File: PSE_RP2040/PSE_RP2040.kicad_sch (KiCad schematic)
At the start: 69 parts, among them J1 USB_B, J2 USB_B_Mini, J3 8P8C_LED, J4 Conn_01x03, Q2 IRLML6402, SW1 SW_Push, SW2 SW_Push, U1 RP2040, U2 PCF8563T, U5 W25Q16JVUSSQ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

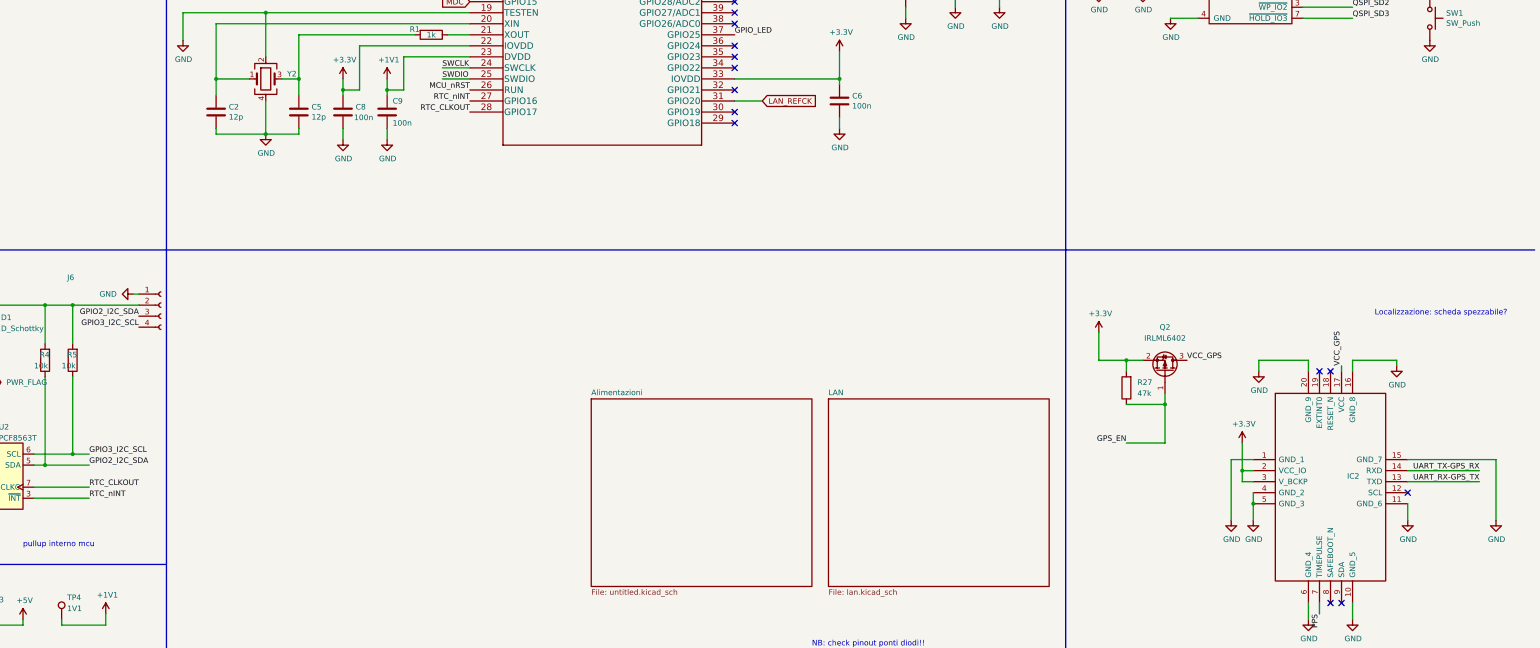
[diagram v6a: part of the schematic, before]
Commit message: piazzamento componenti pcb
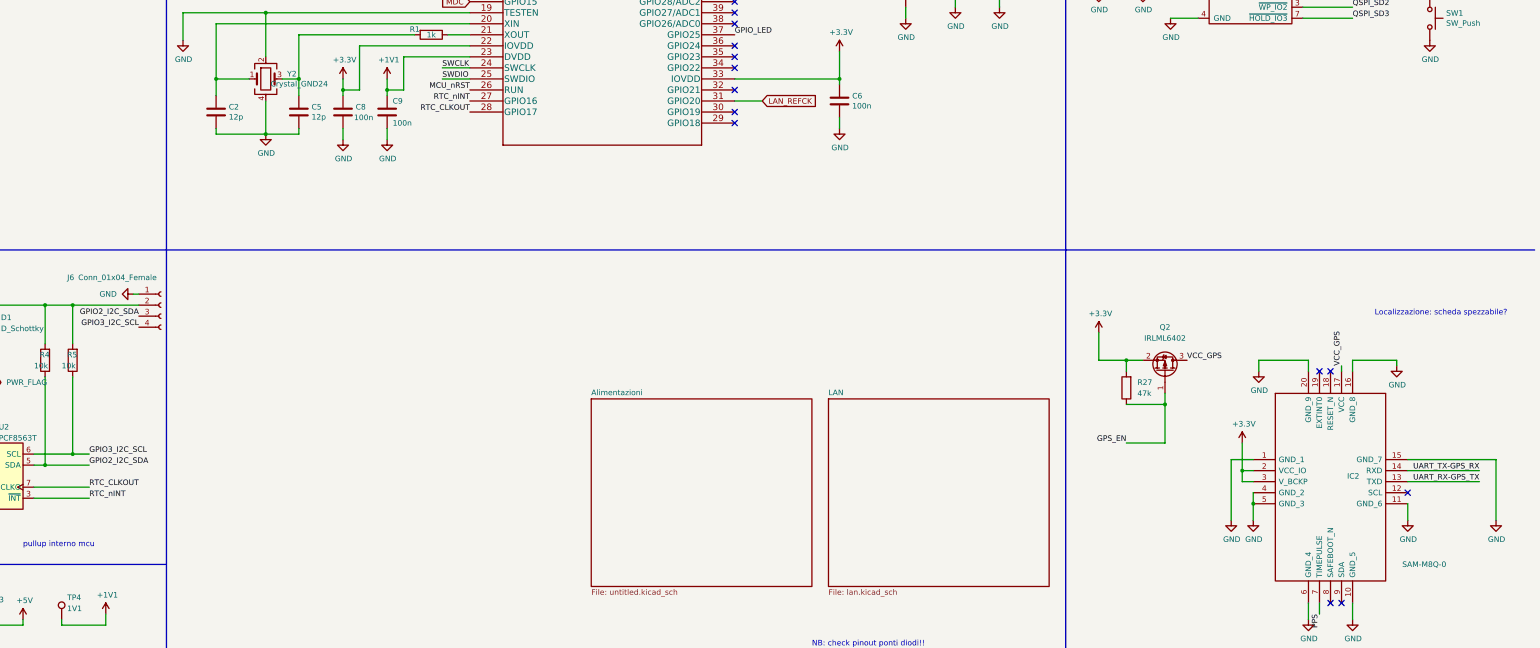
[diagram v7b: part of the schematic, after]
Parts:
- IC2: value (none) -> SAM-M8Q-0; footprint (none) -> PSE2021:SAM-M8Q
- J6: value (none) -> Conn_01x04_Female; footprint (none) -> Connector_PinHeader_2.54mm:PinHeader_1x04_P2.54mm_Vertical
- SW1, SW2: footprint (none) -> Button_Switch_THT:SW_PUSH_6mm
- TP1, TP2: footprint (none) -> TestPoint:TestPoint_Loop_D1.80mm_Drill1.0mm_Beaded
- TP10, TP11, TP12, TP13, TP3, TP4, TP5, TP6, TP7, TP8, TP9: footprint (none) -> TestPoint:TestPoint_Pad_D1.0mm
- Y2: value (none) -> Crystal_GND24; footprint (none) -> Crystal:Crystal_SMD_3225-4Pin_3.2x2.5mm
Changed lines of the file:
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@@
       (effects (font (size 1.27 1.27)) (justify left))
     )
-    (property "Value" "" (id 1) (at 116.6876 87.503 0)
-      (effects (font (size 1.27 1.27)) (justify left))
-    )
-    (property "Footprint" "" (id 2) (at 115.57 86.36 0)
+    (property "Value" "Crystal_GND24" (id 1) (at 116.6876 87.503 0)
+      (effects (font (size 1.27 1.27)) (justify left))
+    )
+    (property "Footprint" "Crystal:Crystal_SMD_3225-4Pin_3.2x2.5mm" (id 2) (at 115.57 86.36 0)
       (effects (font (size 1.27 1.27)) hide)
     )
@@
       (effects (font (size 1.27 1.27)) (justify left))
     )
-    (property "Footprint" "" (id 2) (at 388.62 72.39 0)
+    (property "Footprint" "Button_Switch_THT:SW_PUSH_6mm" (id 2) (at 388.62 72.39 0)
       (effects (font (size 1.27 1.27)) hide)
     )
@@
       (effects (font (size 1.27 1.27)) (justify left))
     )
-    (property "Footprint" "" (id 2) (at 43.18 210.82 0)
+    (property "Footprint" "TestPoint:TestPoint_Loop_D1.80mm_Drill1.0mm_Beaded" (id 2) (at 43.18 210.82 0)
       (effects (font (size 1.27 1.27)) hide)
     )
@@
       (effects (font (size 1.27 1.27)) (justify left))
     )
-    (property "Footprint" "" (id 2) (at 73.66 238.76 0)
+    (property "Footprint" "TestPoint:TestPoint_Pad_D1.0mm" (id 2) (at 73.66 238.76 0)
       (effects (font (size 1.27 1.27)) hide)
     )
@@
       (effects (font (size 1.27 1.27)) (justify left))
     )
-    (property "Footprint" "" (id 2) (at 24.13 255.27 0)
+    (property "Footprint" "TestPoint:TestPoint_Pad_D1.0mm" (id 2) (at 24.13 255.27 0)
       (effects (font (size 1.27 1.27)) hide)
     )
@@
       (effects (font (size 1.27 1.27)) (justify left))
     )
-    (property "Footprint" "" (id 2) (at 24.13 210.82 0)
+    (property "Footprint" "TestPoint:TestPoint_Loop_D1.80mm_Drill1.0mm_Beaded" (id 2) (at 24.13 210.82 0)
       (effects (font (size 1.27 1.27)) hide)
     )
@@
       (effects (font (size 1.27 1.27)) (justify left))
     )
-    (property "Footprint" "" (id 2) (at 24.13 238.76 0)
+    (property "Footprint" "TestPoint:TestPoint_Pad_D1.0mm" (id 2) (at 24.13 238.76 0)
       (effects (font (size 1.27 1.27)) hide)
     )
@@
       (effects (font (size 1.27 1.27)) (justify left))
     )
-    (property "Footprint" "" (id 2) (at 80.01 224.79 0)
+    (property "Footprint" "TestPoint:TestPoint_Pad_D1.0mm" (id 2) (at 80.01 224.79 0)
       (effects (font (size 1.27 1.27)) hide)
     )
@@
       (effects (font (size 1.27 1.27)) (justify left))
     )
-    (property "Footprint" "" (id 2) (at 63.5 224.79 0)
+    (property "Footprint" "TestPoint:TestPoint_Pad_D1.0mm" (id 2) (at 63.5 224.79 0)
       (effects (font (size 1.27 1.27)) hide)
     )
@@
       (effects (font (size 1.27 1.27)) (justify left))
     )
-    (property "Footprint" "" (id 2) (at 44.45 226.06 0)
+    (property "Footprint" "TestPoint:TestPoint_Pad_D1.0mm" (id 2) (at 44.45 226.06 0)
       (effects (font (size 1.27 1.27)) hide)
     )
@@
       (effects (font (size 1.27 1.27)) (justify left))
     )
-    (property "Footprint" "" (id 2) (at 73.66 210.82 0)
+    (property "Footprint" "TestPoint:TestPoint_Pad_D1.0mm" (id 2) (at 73.66 210.82 0)
       (effects (font (size 1.27 1.27)) hide)
     )
@@
       (effects (font (size 1.27 1.27)) (justify left))
     )
-    (property "Footprint" "" (id 2) (at 111.76 39.37 0)
+    (property "Footprint" "Button_Switch_THT:SW_PUSH_6mm" (id 2) (at 111.76 39.37 0)
       (effects (font (size 1.27 1.27)) hide)
     )
@@
       (effects (font (size 1.27 1.27)) (justify left))
     )
-    (property "Footprint" "" (id 2) (at 24.13 226.06 0)
+    (property "Footprint" "TestPoint:TestPoint_Pad_D1.0mm" (id 2) (at 24.13 226.06 0)
       (effects (font (size 1.27 1.27)) hide)
     )
@@
       (effects (font (size 1.27 1.27)) (justify left))
     )
-    (property "Value" "" (id 1) (at 377.19 198.12 0)
-      (effects (font (size 1.27 1.27)) (justify left))
-    )
-    (property "Footprint" "" (id 2) (at 374.65 158.75 0)
+    (property "Value" "SAM-M8Q-0" (id 1) (at 377.19 198.12 0)
+      (effects (font (size 1.27 1.27)) (justify left))
+    )
+    (property "Footprint" "PSE2021:SAM-M8Q" (id 2) (at 374.65 158.75 0)
       (effects (font (size 1.27 1.27)) (justify left) hide)
     )
@@
       (effects (font (size 1.27 1.27)) (justify left))
     )
-    (property "Footprint" "" (id 2) (at 45.72 255.27 0)
+    (property "Footprint" "TestPoint:TestPoint_Pad_D1.0mm" (id 2) (at 45.72 255.27 0)
       (effects (font (size 1.27 1.27)) hide)
     )
@@
       (effects (font (size 1.27 1.27)) (justify left))
     )
-    (property "Footprint" "" (id 2) (at 45.72 238.76 0)
+    (property "Footprint" "TestPoint:TestPoint_Pad_D1.0mm" (id 2) (at 45.72 238.76 0)
       (effects (font (size 1.27 1.27)) hide)
     )
@@
       (effects (font (size 1.27 1.27)) (justify left))
     )
-    (property "Footprint" "" (id 2) (at 54.61 210.82 0)
+    (property "Footprint" "TestPoint:TestPoint_Pad_D1.0mm" (id 2) (at 54.61 210.82 0)
       (effects (font (size 1.27 1.27)) hide)
     )
@@
       (effects (font (size 1.27 1.27)) (justify left))
     )
-    (property "Value" "" (id 1) (at 72.39 132.08 0)
-      (effects (font (size 1.27 1.27)) (justify left))
-    )
-    (property "Footprint" "" (id 2) (at 91.44 138.43 0)
-      (effects (font (size 1.27 1.27)) hide)
-    )
+    (property "Value" "Conn_01x04_Female" (id 1) (at 72.39 132.08 0)
+      (effects (font (size 1.27 1.27)) (justify left))
+    )
+    (property "Footprint" "Connector_PinHeader_2.54mm:PinHeader_1x04_P2.54mm_Vertical" (id 2) (at 91.44 138.43 0)
+      (effects (font (size 1.27 1.27)) hide)
+    )

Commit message: pcb merdaccia
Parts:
- removed C36: 10n, Capacitor_SMD:C_0603_1608Metric, symbol Device:C
- removed R36: 1M, Resistor_SMD:R_0603_1608Metric, symbol Device:R
- C1: value 0.1F -> (none); footprint Capacitor_THT:CP_Radial_D10.0mm_P5.00mm -> (none)
- C10, C11, C13, C15, C3, C6, C7, C8, C9: value 100n -> (none); footprint Capacitor_SMD:C_0603_1608Metric -> (none)
- C12, C14, C18: value 2u2 -> (none); footprint Capacitor_SMD:C_0603_1608Metric -> (none)
- C2, C5: value 12p -> (none); footprint Capacitor_SMD:C_0603_1608Metric -> (none)
- C4: value 10u -> (none); footprint Capacitor_SMD:C_0805_2012Metric -> (none)
- D1: value D_Schottky -> (none); footprint Diode_SMD:D_SMA -> (none)
- D2, D3: value MB1S -> (none); footprint Package_SO:SO-4_4.4x3.6mm_P2.54mm -> (none)
- D4: value LED -> (none); footprint LED_SMD:LED_0603_1608Metric -> (none)
- E1: value SparkGap -> (none); footprint PSE2021:SPARK_GAP_TRIANGLE -> (none)
- H1, H2, H3, H4: value MountingHole -> (none); footprint MountingHole:MountingHole_3mm -> (none)
- IC2: value SAM-M8Q-0 -> (none); footprint PSE2021:SAM-M8Q -> (none)
- J1: value USB_B -> (none); footprint Connector_USB:USB_B_OST_USB-B1HSxx_Horizontal -> (none)
- J2: value USB_B_Mini -> (none); footprint Connector_USB:USB_Mini-B_Wuerth_65100516121_Horizontal -> (none)
- J3: value 8P8C_LED -> (none); footprint PSE2021:RJ45_Amphenol_RJHSE-5081 -> (none)
- J4: value Conn_01x03 -> (none); footprint Connector_PinHeader_2.54mm:PinHeader_1x03_P2.54mm_Vertical -> (none)
- J6: value Conn_01x04_Female -> (none); footprint Connector_PinHeader_2.54mm:PinHeader_1x04_P2.54mm_Vertical -> (none)
- L1: value 200mA 120Ohm -> (none); footprint Inductor_SMD:L_0603_1608Metric -> (none)
- Q2: value IRLML6402 -> (none); footprint Package_TO_SOT_SMD:SOT-23 -> (none)
- R1, R11, R37: value 1k -> (none); footprint Resistor_SMD:R_0603_1608Metric -> (none)
- R12, R13: value 27 -> (none); footprint Resistor_SMD:R_0603_1608Metric -> (none)
- R2: value 100 -> (none); footprint Resistor_SMD:R_0603_1608Metric -> (none)
- R27: value 47k -> (none); footprint Resistor_SMD:R_0603_1608Metric -> (none)
- R28: value R4 no fit (o 10k) -> (none); footprint Resistor_SMD:R_0603_1608Metric -> (none)
- R3: value R -> (none); footprint Resistor_SMD:R_0603_1608Metric -> (none)
- R4, R5: value 10k -> (none); footprint Resistor_SMD:R_0603_1608Metric -> (none)
- R6, R7: value 270 -> (none); footprint Resistor_SMD:R_0603_1608Metric -> (none)
- SW1, SW2: value SW_Push -> (none); footprint Button_Switch_THT:SW_PUSH_6mm -> (none)
- TP1: value 3V3 -> (none); footprint TestPoint:TestPoint_Loop_D1.80mm_Drill1.0mm_Beaded -> (none)
- TP10: value UART_RX-GPS_TX -> (none); footprint TestPoint:TestPoint_Pad_D1.0mm -> (none)
- TP11: value VCC_GPS -> (none); footprint TestPoint:TestPoint_Pad_D1.0mm -> (none)
- TP12: value I2C_SCL_RTC -> (none); footprint TestPoint:TestPoint_Pad_D1.0mm -> (none)
- TP13: value I2C_SDA_RTC -> (none); footprint TestPoint:TestPoint_Pad_D1.0mm -> (none)
- TP2: value GND -> (none); footprint TestPoint:TestPoint_Loop_D1.80mm_Drill1.0mm_Beaded -> (none)
- TP3: value 5V -> (none); footprint TestPoint:TestPoint_Pad_D1.0mm -> (none)
- TP4: value 1V1 -> (none); footprint TestPoint:TestPoint_Pad_D1.0mm -> (none)
- TP5: value POE+ -> (none); footprint TestPoint:TestPoint_Pad_D1.0mm -> (none)
- TP6: value POE- -> (none); footprint TestPoint:TestPoint_Pad_D1.0mm -> (none)
- TP7: value USB_DP -> (none); footprint TestPoint:TestPoint_Pad_D1.0mm -> (none)
- TP8: value USB_DN -> (none); footprint TestPoint:TestPoint_Pad_D1.0mm -> (none)
- TP9: value UART_TX-GPS_RX -> (none); footprint TestPoint:TestPoint_Pad_D1.0mm -> (none)
- U1: value RP2040 -> (none); footprint PSE2021:RP2040-QFN-56 -> (none)
- U2: value PCF8563T -> (none); footprint Package_SO:SOIC-8_3.9x4.9mm_P1.27mm -> (none)
- U5: value W25Q16JVUSSQ -> (none); footprint Package_SO:SOIC-8_5.275x5.275mm_P1.27mm -> (none)
- U6: value PAM7Q -> (none); footprint PSE2021:PAM-7Q -> (none)
- Y1: value Crystal_GND3 -> (none); footprint Crystal:Crystal_AT310_D3.0mm_L10.0mm_Horizontal_1EP_style1 -> (none)
- Y2: value Crystal_GND24 -> (none); footprint Crystal:Crystal_SMD_3225-4Pin_3.2x2.5mm -> (none)
